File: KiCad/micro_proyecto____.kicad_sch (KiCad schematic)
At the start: 33 parts, among them J1 Conn_01x05, J2 Conn_01x02, J3 Conn_01x02, J4 Conn_01x02, J5 Conn_01x02, SW1 SW_Push, SW2 SW_SPST, SW3 SW_SPST, SW4 SW_SPST, SW5 SW_SPST, U1 PIC24HJ128GP502, Y1 Crystal

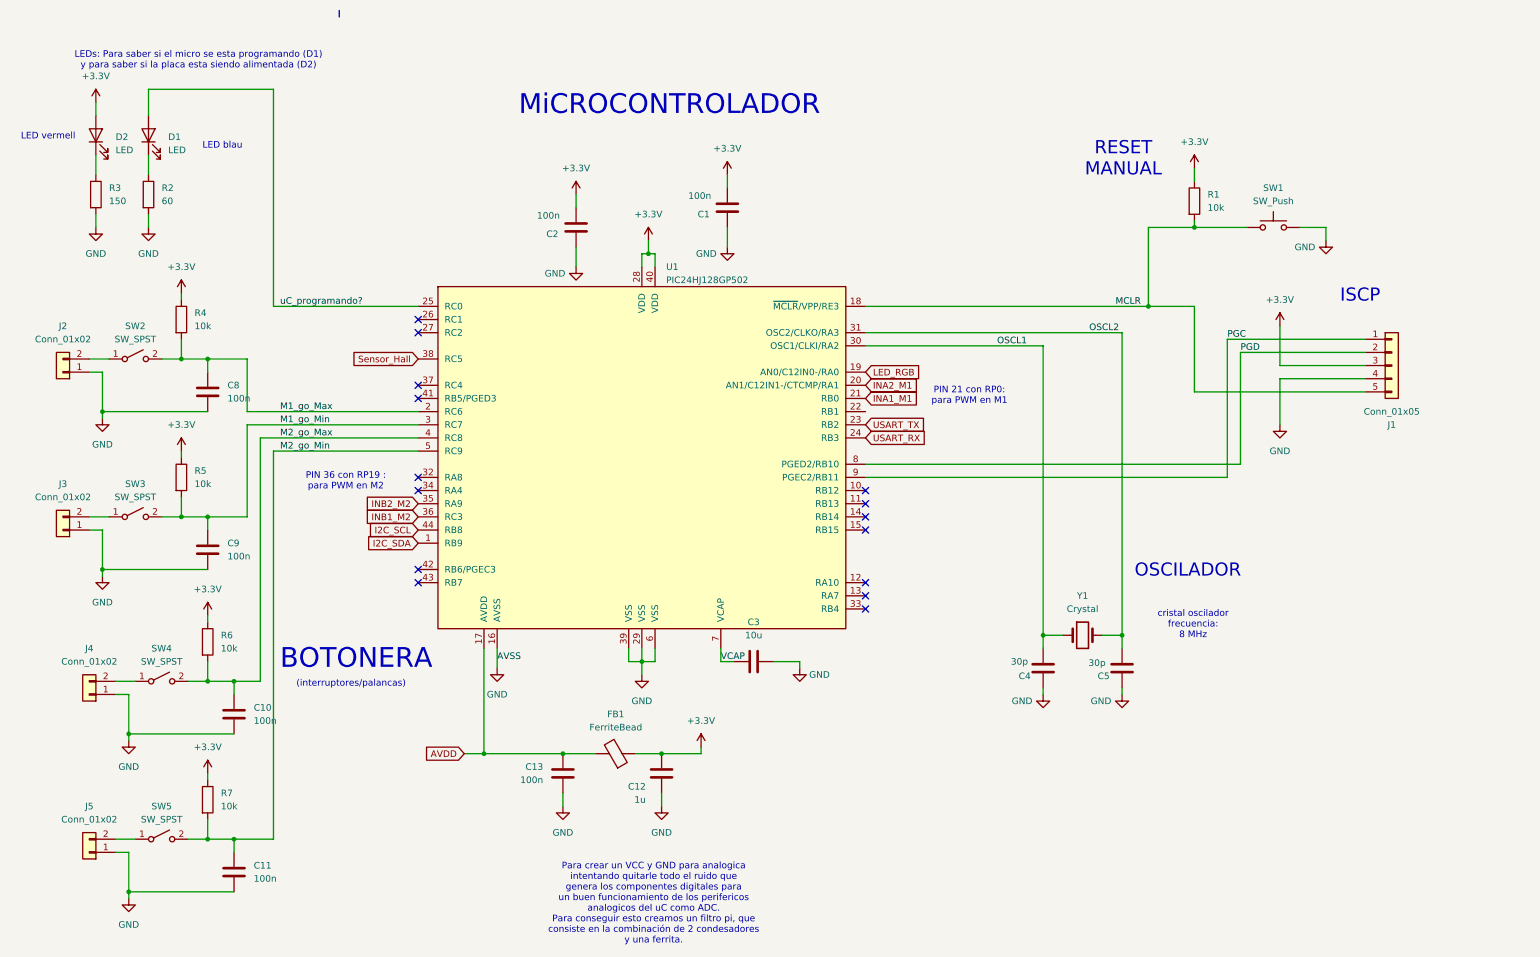
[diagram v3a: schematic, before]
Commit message: Esquematico cambio en Sensor final de Carrera y Readme
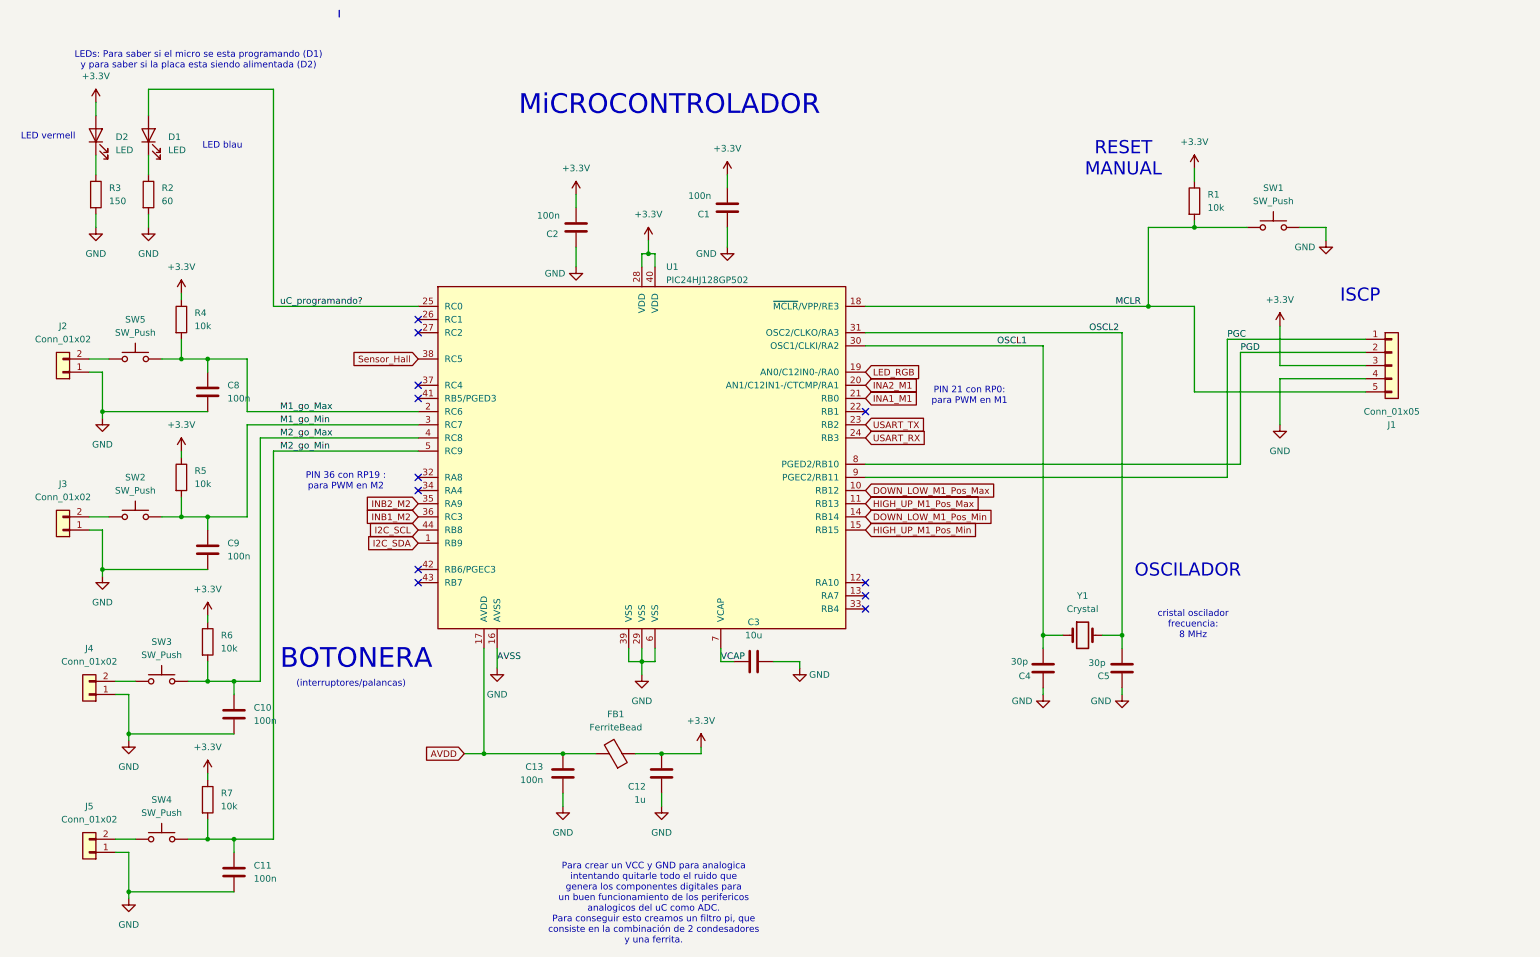
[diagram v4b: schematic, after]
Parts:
- removed SW2, SW3, SW4, SW5: SW_SPST, Button_Switch_THT:SW_SPST_Omron_B3F-50xx, symbol Switch:SW_SPST
- added SW2, SW3, SW4, SW5: SW_Push, Button_Switch_THT:SW_PUSH_6mm, symbol Switch:SW_Push
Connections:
- net M1_go_Max: now also SW5.2
- net M1_go_Min: now also SW2.2
- net M2_go_Max: now also SW3.2
- net M2_go_Min: now also SW4.2
- net at J4.2 (Pin_2): now also SW3.1
- net at J5.2 (Pin_2): now also SW4.1
- net at J2.2 (Pin_2): now also SW5.1
- net at J3.2 (Pin_2): now also SW2.1
- net DOWN_LOW_M1_Pos_Max: now reaches U1.10 (RB12)
- net HIGH_UP_M1_Pos_Max: now reaches U1.11 (RB13)
- net DOWN_LOW_M1_Pos_Min: now reaches U1.14 (RB14)
- net HIGH_UP_M1_Pos_Min: now reaches U1.15 (RB15)
- no-connect marks 15 -> 12

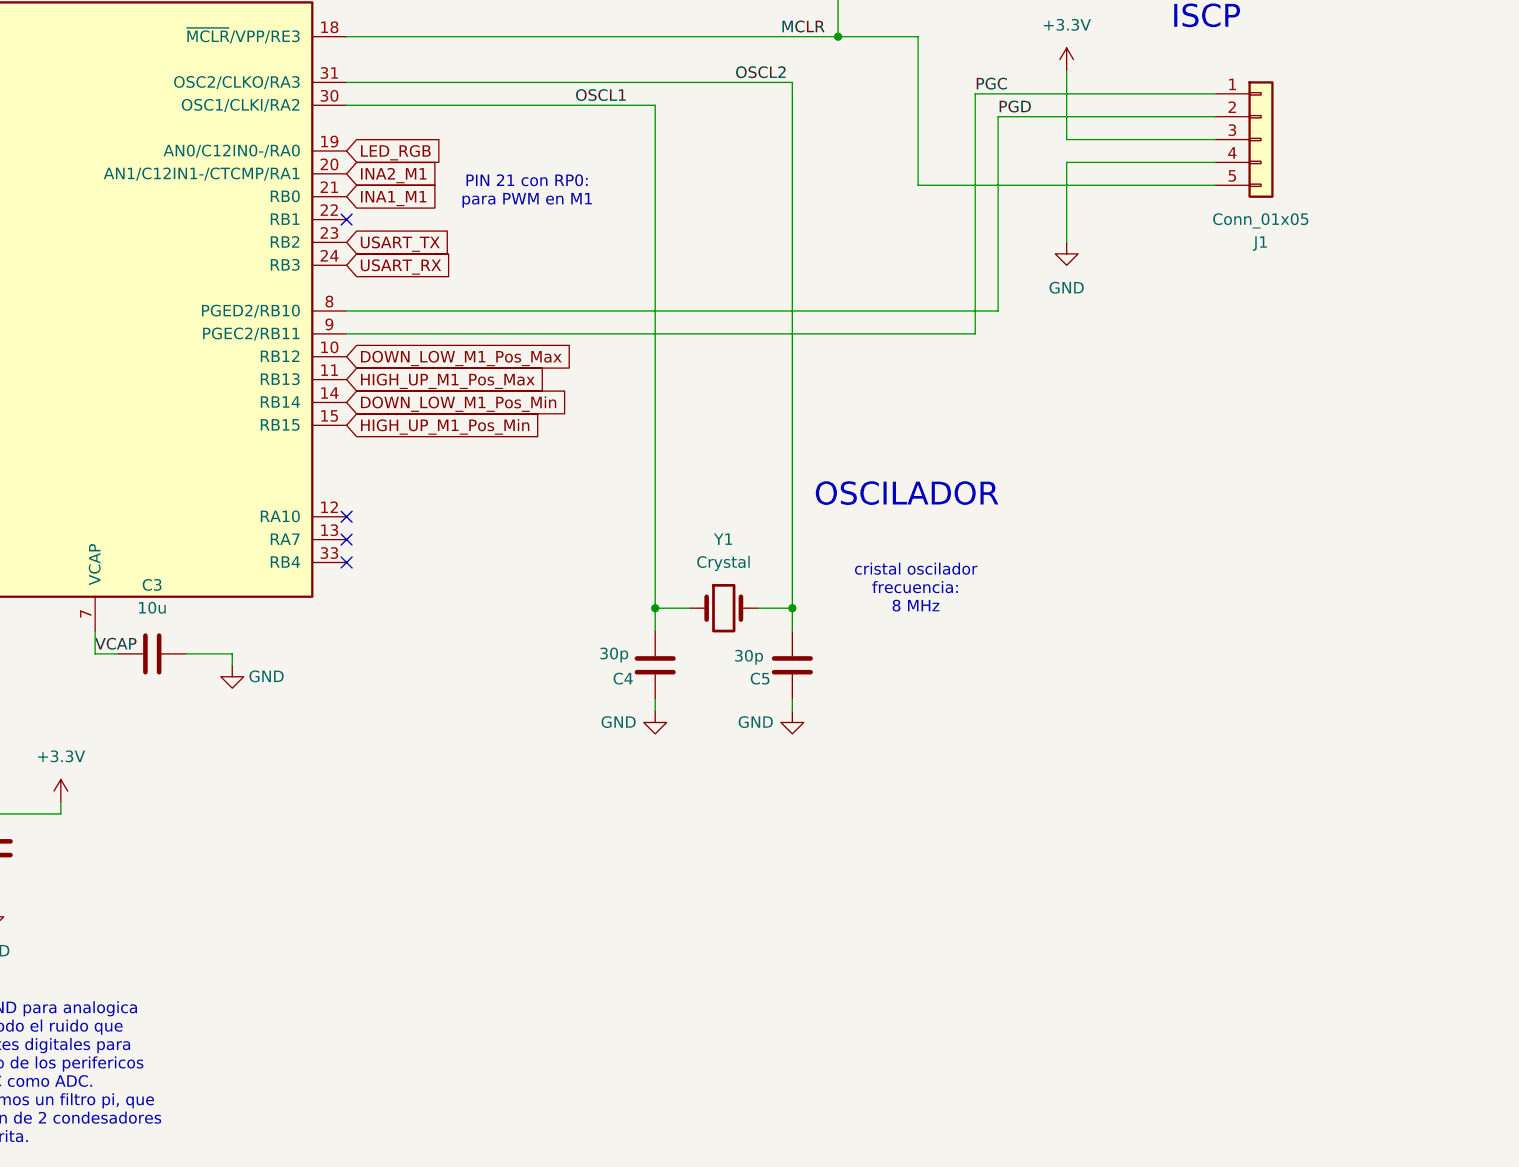
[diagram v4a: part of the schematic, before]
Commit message: Esquematico acabado y readme estructura base y componentes acabado y puesto el DB.
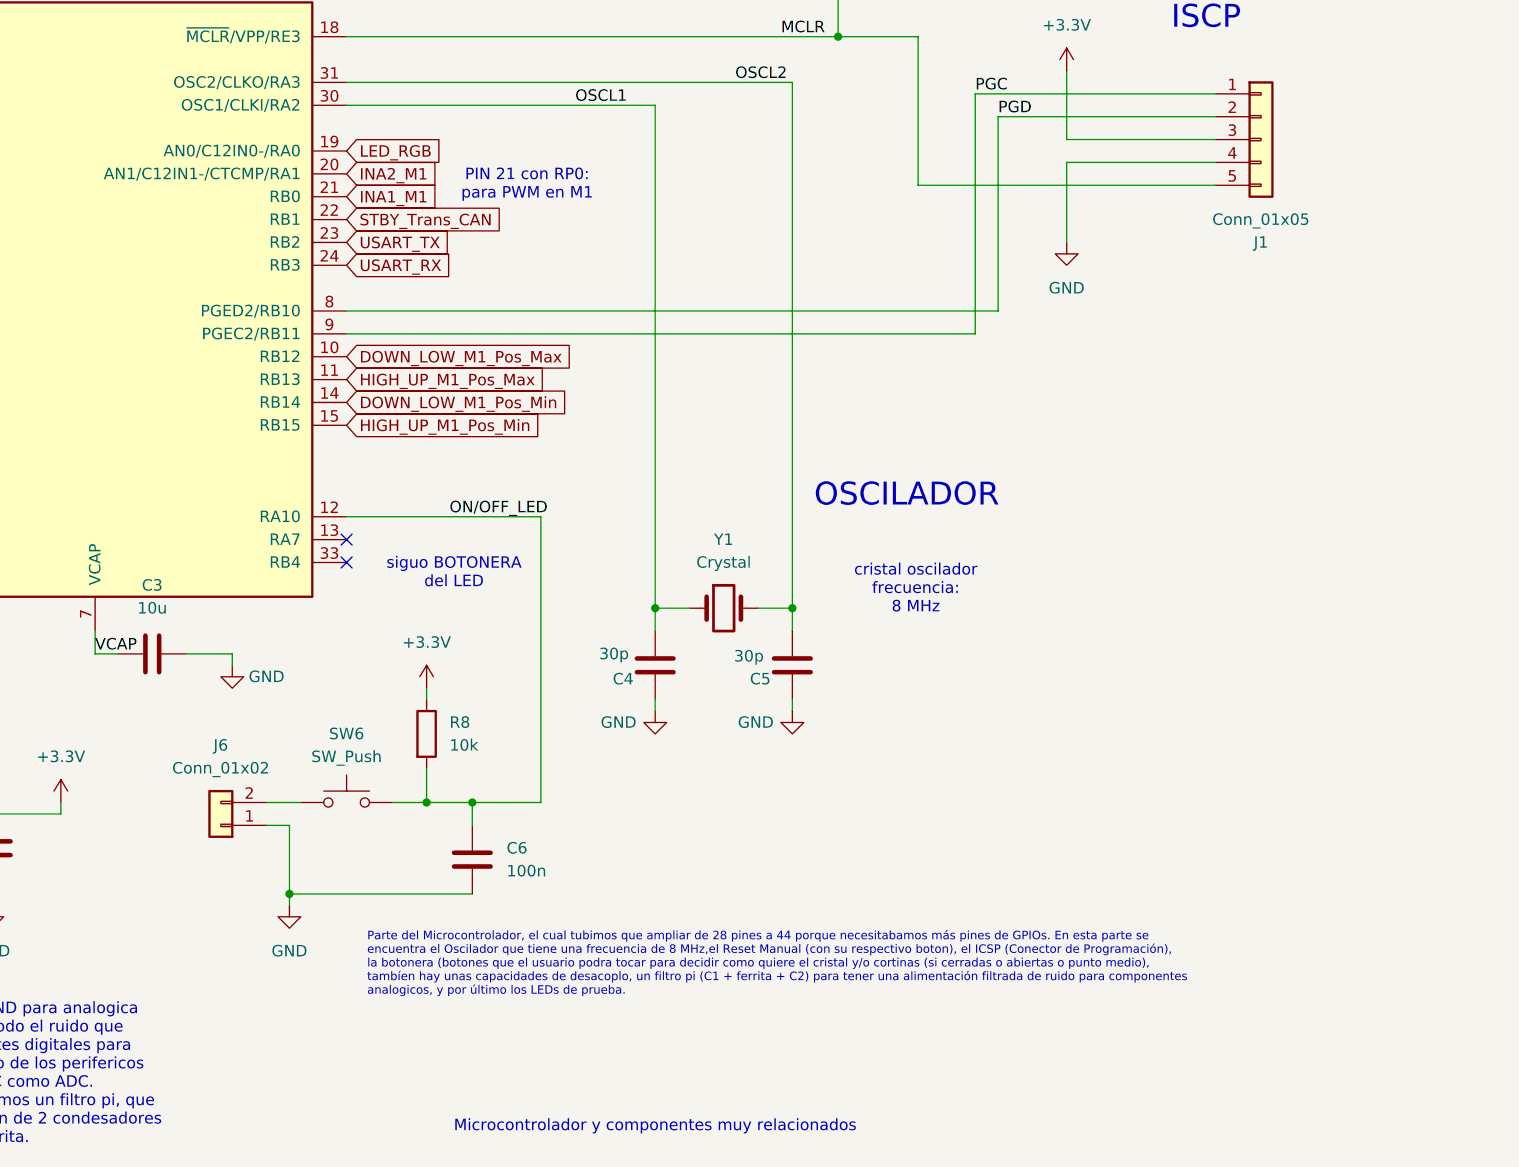
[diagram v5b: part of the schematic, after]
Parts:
- added C6: 100n, Capacitor_SMD:C_0805_2012Metric, symbol Device:C
- added J6: Conn_01x02, Connector_PinHeader_2.54mm:PinHeader_1x02_P2.54mm_Horizontal, symbol Connector_Generic:Conn_01x02
- added R8: 10k, Resistor_SMD:R_0805_2012Metric, symbol Device:R
- added SW6: SW_Push, Button_Switch_THT:SW_PUSH_6mm, symbol Switch:SW_Push
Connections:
- net +3.3V: now also R8.1
- net GND: now also C6.2, J6.1 (Pin_1)
- net ON/OFF_LED: now reaches U1.12 (RA10)
- net ON/OFF_LED: now also C6.1, R8.2, SW6.2
- net STBY_Trans_CAN: now reaches U1.22 (RB1)
- new net: J6.2 (Pin_2), SW6.1
- no-connect marks 12 -> 10
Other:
- note added: "Microcontrolador y componentes muy relacionados"
- note added: "Parte del Microcontrolador, el cual tubimos que ampliar de 28 pines a 44 porque necesitabamos más pines de GPIOs. En esta parte se encuentra el Oscilador que tiene una frecuencia de 8 MHz,el Reset Manual (con su respectivo boton), el ICSP (Conector de Programación), la botonera (botones que el usuario podra tocar para decidir como quiere el cristal y/o cortinas (si cerradas o abiertas o punto med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"
- note added: "siguo BOTONERA del LED"

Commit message: Cambios al esquematico por SEsión 3
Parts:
- Y1: footprint Crystal:Crystal_SMD_7050-2Pin_7.0x5.0mm_HandSoldering -> Crystal:Crystal_HC52-6mm_Vertical
- renumbered C8 to C1, C12 to C10, C1 to C11, C6 to C12, C9 to C2, C2 to C3, C3 to C4, C4 to C5, C5 to C6, C10 to C7, C11 to C8, C13 to C9, D2 to D1, D1 to D2, J2 to J1, J1 to J2, R3 to R2, R2 to R3, SW5 to SW2, SW2 to SW3, SW3 to SW4, SW4 to SW5, U1 to U4

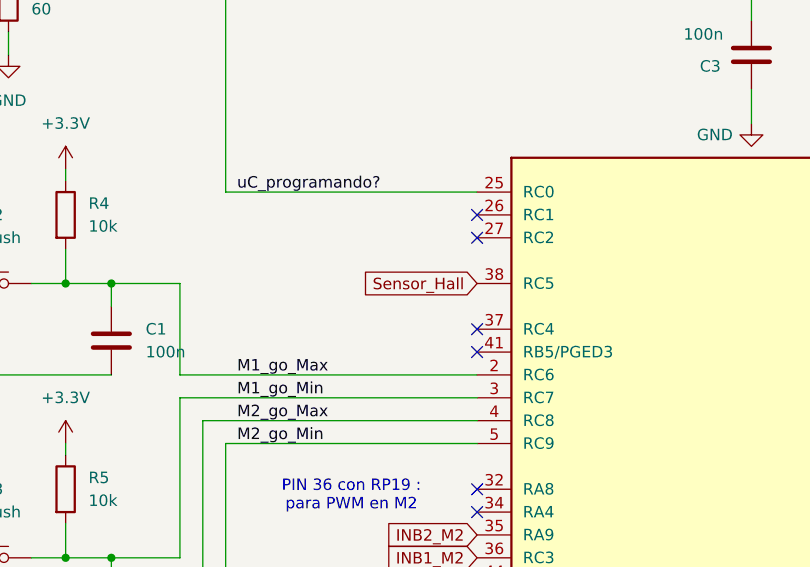
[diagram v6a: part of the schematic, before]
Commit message: Cambio DG y pinzeladas ultimas al esquematico
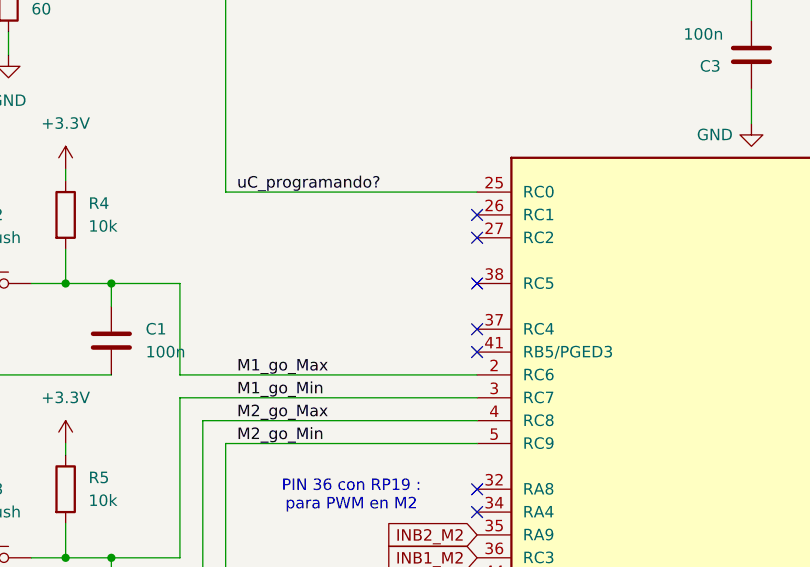
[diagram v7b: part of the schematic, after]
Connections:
- net Sensor_Hall: no longer names the net of U4.38 (RC5)
- no-connect marks 10 -> 11
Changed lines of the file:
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@@
+	)
+	(no_connect
+		(at 90.17 78.74)
 	)
 	(no_connect
@@
 				(hide yes)
 			)
-		)
-	)
-	(global_label "Sensor_Hall"
-		(shape input)
-		(at 90.17 78.74 180)
-		(fields_autoplaced yes)
-		(effects
-			(font
-				(size 1.27 1.27)
-			)
-			(justify right)
-		)
-		(property "Intersheetrefs" "${INTERSHEET_REFS}"
-			(at 75.9969 78.74 0)
-			(effects
-				(font
-					(size 1.27 1.27)
-				)
-				(justify right)
-				(hide yes)
-			)
